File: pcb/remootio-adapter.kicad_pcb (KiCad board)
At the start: 2 copper layers, 110 x 60 mm, 63 parts, among them J1 AUX, J2 BATT, J3 ICSP, J4 Console, J5 SwitchIn, J6 SPM Connector, U1 remootio-3, U2 LM2940S-5.0, U3 AQV252GAX, U4 ATmega328PB-ANR, U5 ST232CDR, U6 AQV252GAX, U7 AQV252GAX, U8 AQV252GAX, Y1 CSTCE16M0V53-R0

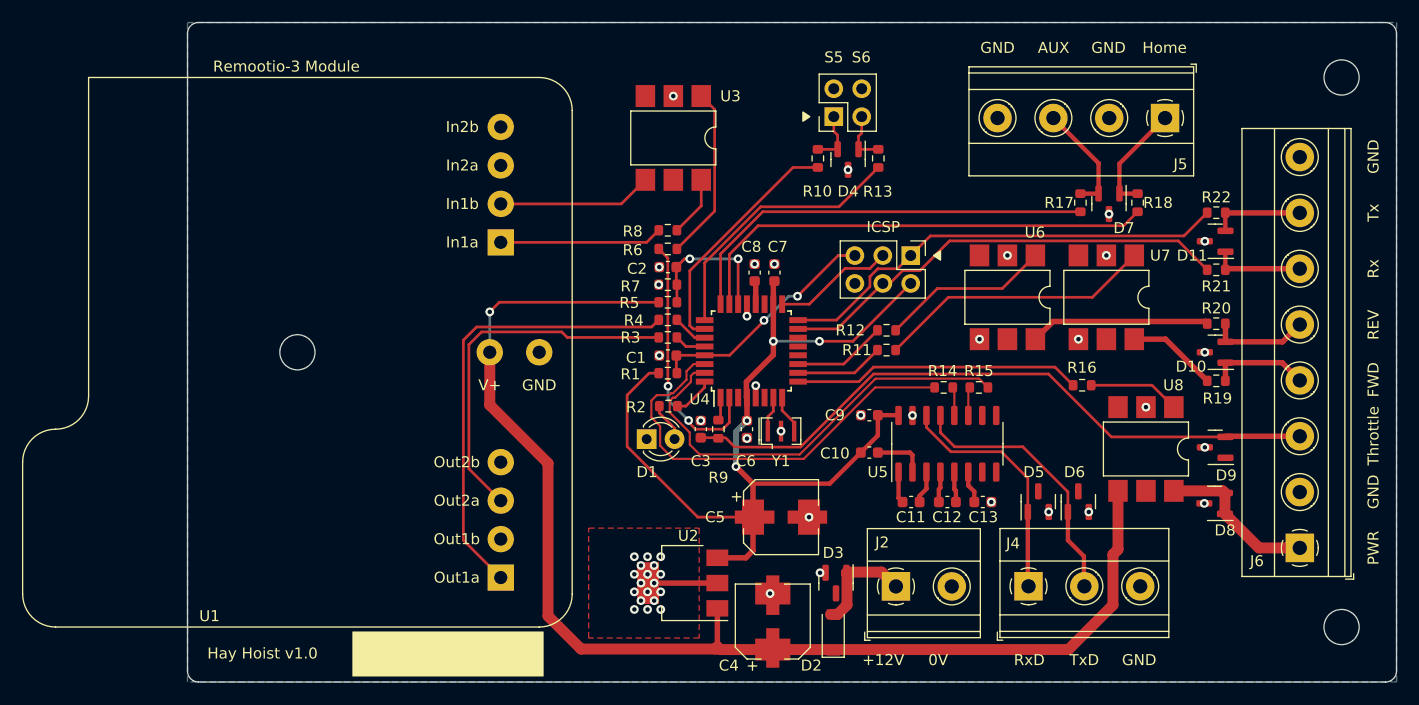
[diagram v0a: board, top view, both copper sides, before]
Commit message: Revise PCB layout for production board v1.1
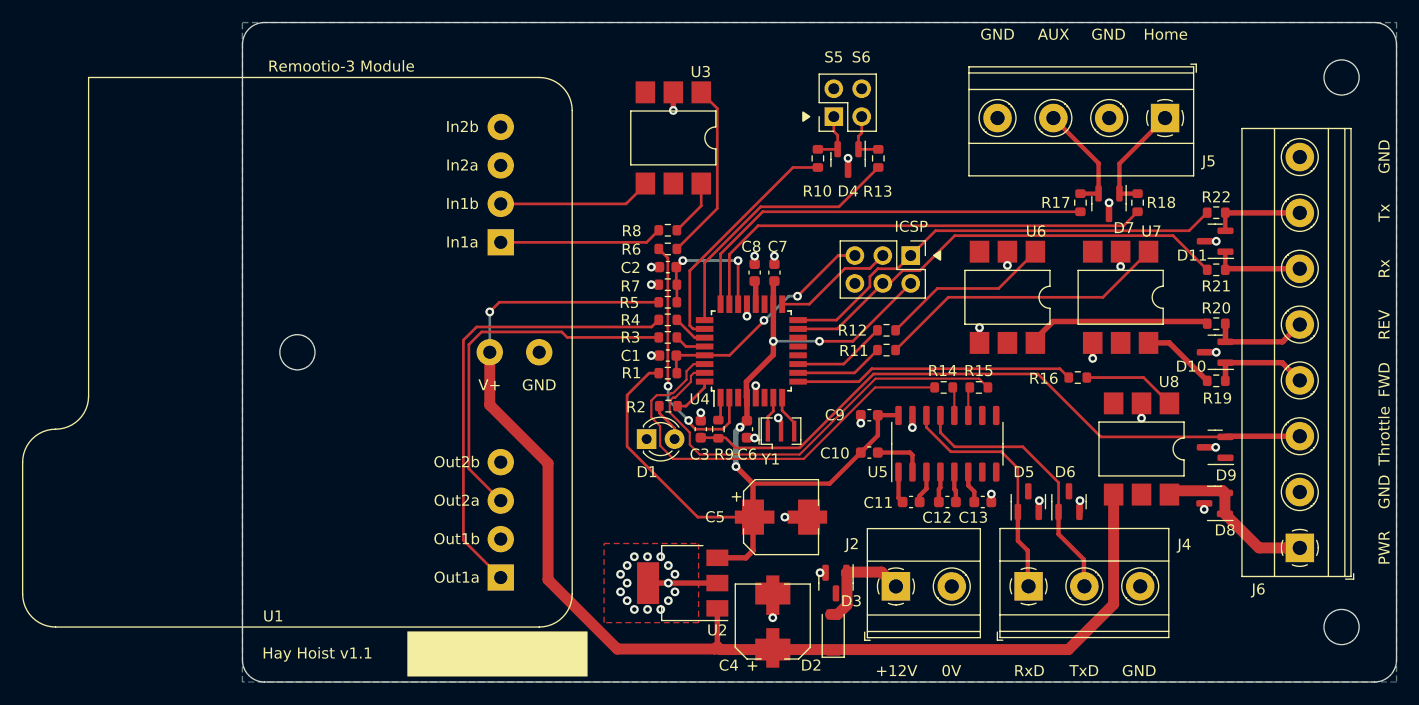
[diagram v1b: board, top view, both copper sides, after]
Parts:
- C1: value 1µ -> 100nF
- R1: value 1k -> 4.7k
- U3, U6, U7, U8: footprint Package_DIP:SMDIP-6_W7.62mm -> remootio-adapter:SMDIP-6_W7.62mm
- moved U7 1.30 mm to (156.9, 92.0)
- moved D5 0.91 mm to (148.5, 110.6)
- moved D6 0.85 mm to (152.2, 110.6)
- moved R16 0.81 mm to (153.0, 99.3)
- moved U8 0.40 mm to (158.8, 105.8)
- turned R1 to 0 degrees
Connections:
- R1 pad 1: RESET -> +5V
- R1 pad 2: +5V -> RESET
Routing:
- net GND: track 7.83 -> 36.6 mm, vias 48 -> 46
- net +12V: track 114.2 -> 111.8 mm
- net Net-(R19-Pad1): track 8.20 -> 6.76 mm
- net Net-(R11-Pad2): track 25.3 -> 26.7 mm
- net R3: track 26.3 -> 25.4 mm
- net Net-(R6-Pad2): track 15.8 -> 16.4 mm
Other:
- board size 110 x 60 mm -> 105 x 60 mm
- board text added: "Hay Hoist v1.1"
- board text removed: "Hay Hoist v1.0"

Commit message: Add mounting hole diagram
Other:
- board text added: "Antenna Clearance"
- board text added: "Connector Clearance"
- board text added: "M3"
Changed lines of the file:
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@@
   )
   (paper "A4")
+  (title_block
+    (title "Hay Hoist")
+    (date "2024-07-31")
+    (rev "1.1")
+    (company "Hyspec/6-v")
+  )
   (layers
     (0 "F.Cu" signal)
@@
   (gr_line (start 79 127) (end 180 127) (layer "Edge.Cuts") (width 0.1))
   (gr_line (start 77 69) (end 77 125) (layer "Edge.Cuts") (width 0.1))
+  (gr_line (start 82 96) (end 82 98) (layer "User.2") (width 0.15))
+  (gr_line (start 57 93) (end 64 86) (layer "User.2") (width 0.15))
+  (gr_line (start 164 133) (end 168 129) (layer "User.2") (width 0.15))
+  (gr_poly
+    (pts
+      (xy 189 134)
+      (xy 133 134)
+      (xy 133 128)
+      (xy 183 128)
+      (xy 183 66)
+      (xy 142 66)
+      (xy 142 60)
+      (xy 189 60)
+    ) (layer "User.2") (width 0.15) (fill none))
+  (gr_rect (start 55 70) (end 76 124) (layer "User.2") (width 0.15) (fill none))
+  (gr_line (start 158 133) (end 162 129) (layer "User.2") (width 0.15))
+  (gr_line (start 138 133) (end 140 131) (layer "User.2") (width 0.15))
+  (gr_line (start 176 122) (end 178 122) (layer "User.2") (width 0.15))
+  (gr_line (start 81 97) (end 83 97) (layer "User.2") (width 0.15))
+  (gr_circle (center 82 97) (end 84 97) (layer "User.2") (width 0.15) (fill none))
+  (gr_line (start 68 93) (end 73 88) (layer "User.2") (width 0.15))
+  (gr_circle (center 177 122) (end 179 122) (layer "User.2") (width 0.15) (fill none))
+  (gr_circle (center 177 72) (end 179 72) (layer "User.2") (width 0.15) (fill none))
+  (gr_line (start 177 121) (end 177 123) (layer "User.2") (width 0.15))
+  (gr_line (start 134 133) (end 138 129) (layer "User.2") (width 0.15))
+  (gr_line (start 70 81) (end 74 77) (layer "User.2") (width 0.15))
+  (gr_line (start 61 81) (end 70 72) (layer "User.2") (width 0.15))
+  (gr_rect (start 190 59) (end 54 135) (layer "User.2") (width 0.15) (fill none))
+  (gr_line (start 174 70) (end 173 69) (layer "User.2") (width 0.15))
+  (gr_line (start 84 99) (end 85 100) (layer "User.2") (width 0.15))
+  (gr_line (start 176 72) (end 178 72) (layer "User.2") (width 0.15))
+  (gr_line (start 175 124) (end 174 125) (layer "User.2") (width 0.15))
+  (gr_line (start 177 71) (end 177 73) (layer "User.2") (width 0.15))
+  (gr_line (start 57 77) (end 62 72) (layer "User.2") (width 0.15))
   (gr_text "S5" (at 130.8 70.1625) (layer "F.SilkS")
     (effects (font (size 1 1) (thickness 0.15)))
@@
     (effects (font (size 1 1) (thickness 0.15)))
   )
+  (gr_text "M3" (at 86 101) (layer "User.2")
+    (effects (font (size 1 1) (thickness 0.15)))
+  )
+  (gr_text "M3" (at 171 69) (layer "User.2")
+    (effects (font (size 1 1) (thickness 0.15)))
+  )
+  (gr_text "Connector Clearance" (at 149 131) (layer "User.2")
+    (effects (font (size 1 1) (thickness 0.15)))
+  )
+  (gr_text "M3" (at 172 126) (layer "User.2")
+    (effects (font (size 1 1) (thickness 0.15)))
+  )
+  (gr_text "Antenna Clearance" (at 66 83) (layer "User.2")
+    (effects (font (size 1 1) (thickness 0.15)))
+  )
+  (dimension (type aligned) (layer "User.2")
+    (pts (xy 177 135) (xy 190 135))
+    (height 3)
+    (gr_text "13.0 mm" (at 183.5 140) (layer "User.2")
+      (effects (font (size 1 1) (thickness 0.15)))
+    )
+    (format (units 3) (units_format 1) (precision 1))
+    (style (thickness 0.15) (arrow_length 1.27) (text_position_mode 2) (extension_height 0.58642) (extension_offset 0.5) keep_text_aligned)
+  )
+  (dimension (type aligned) (layer "User.2")
+    (pts (xy 54 59) (xy 54 135))
+    (height 5)
+    (gr_text "76.0 mm" (at 50 96 90) (layer "User.2")
+      (effects (font (size 1 1) (thickness 0.15)))
+    )
+    (format (units 3) (units_format 1) (precision 1))
+    (style (thickness 0.15) (arrow_length 1.27) (text_position_mode 2) (extension_height 0.58642) (extension_offset 0.5) keep_text_aligned)
+  )
+  (dimension (type aligned) (layer "User.2")
+    (pts (xy 190 122) (xy 190 97))
+    (height 6)
+    (gr_text "25.0 mm" (at 194 109.5 90) (layer "User.2")
+      (effects (font (size 1 1) (thickness 0.15)))
+    )
+    (format (units 3) (units_format 1) (precision 1))
+    (style (thickness 0.15) (arrow_length 1.27) (text_position_mode 2) (extension_height 0.58642) (extension_offset 0.5) keep_text_aligned)
+  )
+  (dimension (type aligned) (layer "User.2")
+    (pts (xy 177 135) (xy 82 135))
+    (height -5)
+    (gr_text "95.0 mm" (at 129.5 138.85) (layer "User.2")
+      (effects (font (size 1 1) (thickness 0.15)))
+    )
+    (format (units 3) (units_format 1) (precision 1))
+    (style (thickness 0.15) (arrow_length 1.27) (text_position_mode 0) (extension_height 0.58642) (extension_offset 0.5) keep_text_aligned)
+  )
+  (dimension (type aligned) (layer "User.2")
+    (pts (xy 190 135) (xy 190 122))
+    (height 4)
+    (gr_text "13.0 mm" (at 196 128.5 90) (layer "User.2")
+      (effects (font (size 1 1) (thickness 0.15)))
+    )
+    (format (units 3) (units_format 1) (precision 1))
+    (style (thickness 0.15) (arrow_length 1.27) (text_position_mode 2) (extension_height 0.58642) (extension_offset 0.5) keep_text_aligned)
+  )
+  (dimension (type aligned) (layer "User.2")
+    (pts (xy 54 59) (xy 190 59))
+    (height -4)
+    (gr_text "136.0 mm" (at 122 53.85) (layer "User.2")
+      (effects (font (size 1 1) (thickness 0.15)))
+    )
+    (format (units 3) (units_format 1) (precision 1))
+    (style (thickness 0.15) (arrow_length 1.27) (text_position_mode 0) (extension_height 0.58642) (extension_offset 0.5) keep_text_aligned)
+  )
+  (dimension (type aligned) (layer "User.2")
+    (pts (xy 82 135) (xy 54 135))
+    (height -3)
+    (gr_text "28.0 mm" (at 69 140) (layer "User.2")
+      (effects (font (size 1 1) (thickness 0.15)))
+    )
+    (format (units 3) (units_format 1) (precision 1))
+    (style (thickness 0.15) (arrow_length 1.27) (text_position_mode 2) (extension_height 0.58642) (extension_offset 0.5) keep_text_aligned)
+  )
+  (dimension (type aligned) (layer "User.2")
+    (pts (xy 190 59) (xy 190 67))
+    (height -2)
+    (gr_text "8.0 mm" (at 194 63 90) (layer "User.2")
+      (effects (font (size 1 1) (thickness 0.15)))
+    )
+    (format (units 3) (units_format 1) (precision 1))
+    (style (thickness 0.15) (arrow_length 1.27) (text_position_mode 2) (extension_height 0.58642) (extension_offset 0.5) keep_text_aligned)
+  )
   (segment (start 120.005112 124) (end 111.1 124) (width 1) (layer "F.Cu") (net 1))

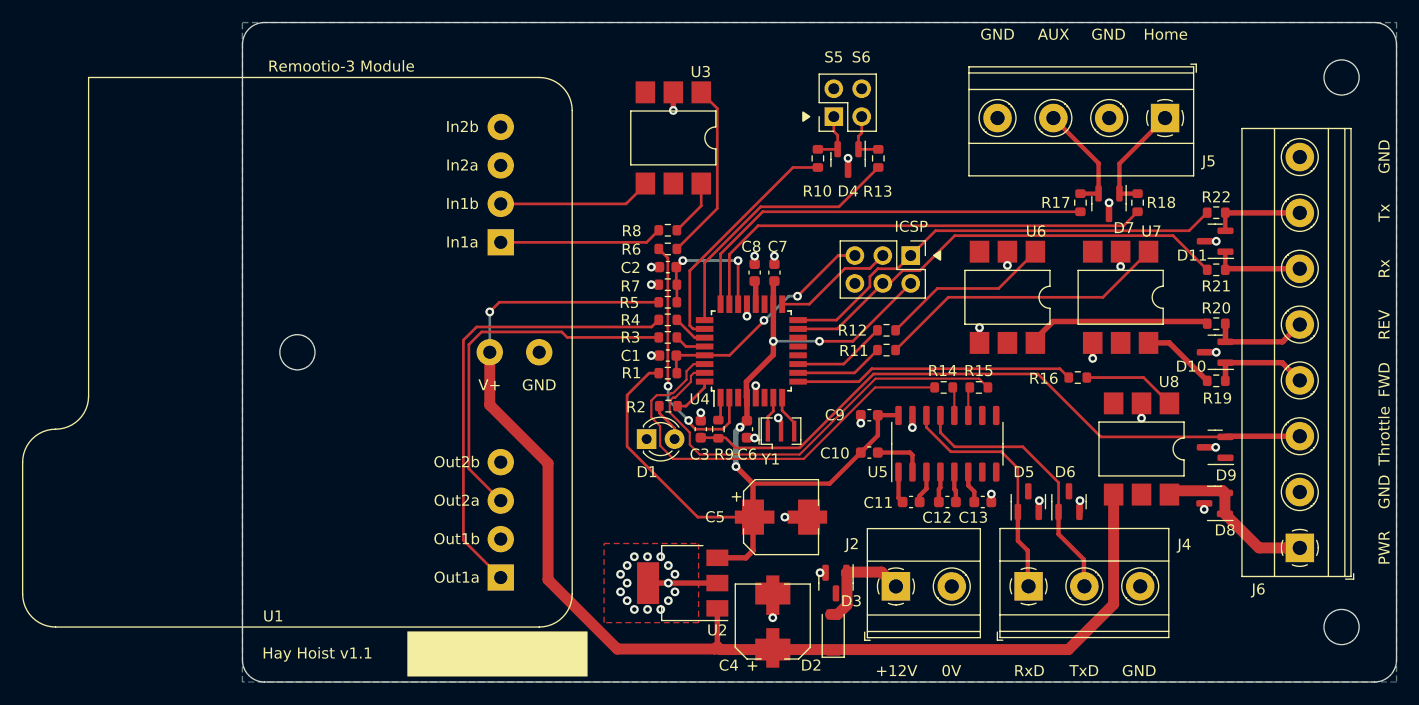
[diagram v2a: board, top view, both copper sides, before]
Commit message: Minor cosmetic footprint adjustment
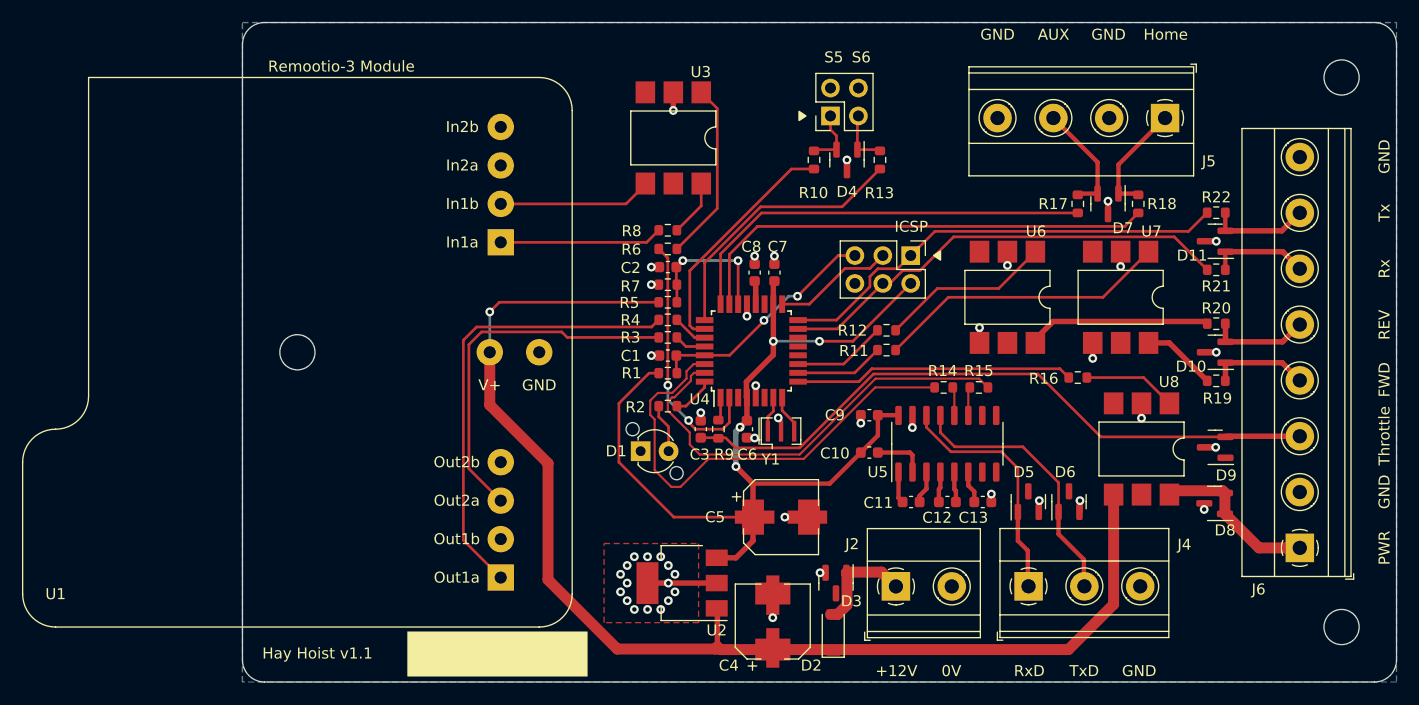
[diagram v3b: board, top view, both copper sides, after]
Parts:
- D1: footprint LED_THT:LED_D3.0mm_Clear -> remootio-adapter:bivar-led
- moved D1 1.32 mm to (114.5, 106.0)
- moved R10 0.38 mm to (129.0, 79.5)
- moved J1 0.31 mm to (130.5, 75.5)
- moved R17 0.26 mm to (153.0, 83.5)
- moved R13 0.20 mm to (135.0, 79.5)
- moved R18 0.13 mm to (158.5, 83.5)
- moved D4 0.11 mm to (132.0, 79.5)
- moved D7 0.09 mm to (155.8, 83.5)
- moved U2 0.06 mm to (117.0, 118.0)
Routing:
- net CRX: track 39.3 -> 43.1 mm
- net +5V: track 84.1 -> 85.5 mm
- net Net-(D1-Pad2): track 3.58 -> 4.47 mm
- net Net-(D11-Pad1): track 8.31 -> 9.04 mm
- net Net-(D11-Pad2): track 8.39 -> 9.08 mm

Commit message: Jostle footprints onto 0.5mm grid and change terminals to 5mm pitch
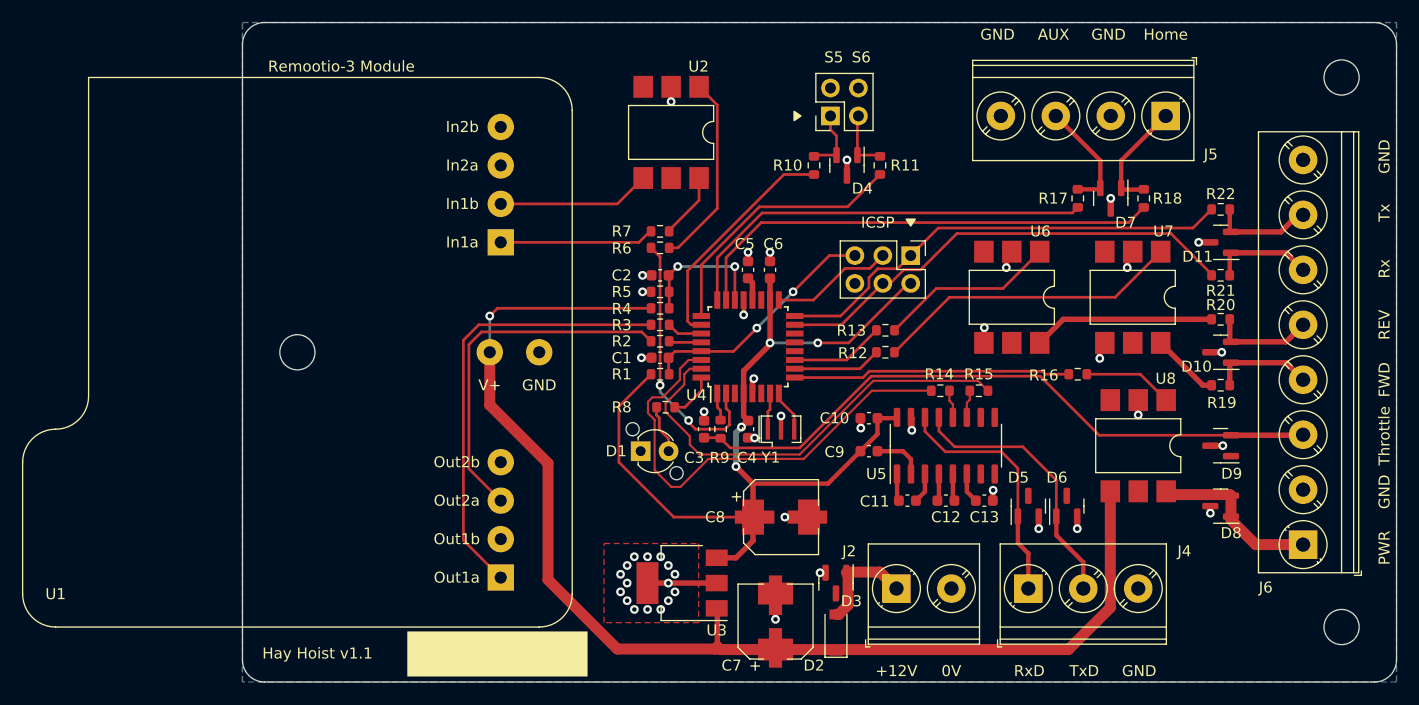
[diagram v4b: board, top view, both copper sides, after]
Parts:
- J2: footprint TerminalBlock_Phoenix:TerminalBlock_Phoenix_MKDS-1,5-2-5.08_1x02_P5.08mm_Horizontal -> TerminalBlock_Phoenix:TerminalBlock_Phoenix_PT-1,5-2-5.0-H_1x02_P5.00mm_Horizontal
- J4: footprint TerminalBlock_Phoenix:TerminalBlock_Phoenix_MKDS-1,5-3-5.08_1x03_P5.08mm_Horizontal -> TerminalBlock_Phoenix:TerminalBlock_Phoenix_PT-1,5-3-5.0-H_1x03_P5.00mm_Horizontal
- J5: footprint TerminalBlock_Phoenix:TerminalBlock_Phoenix_MKDS-1,5-4-5.08_1x04_P5.08mm_Horizontal -> TerminalBlock_Phoenix:TerminalBlock_Phoenix_PT-1,5-4-5.0-H_1x04_P5.00mm_Horizontal
- J6: footprint TerminalBlock_Phoenix:TerminalBlock_Phoenix_MKDS-1,5-8-5.08_1x08_P5.08mm_Horizontal -> TerminalBlock_Phoenix:TerminalBlock_Phoenix_PT-1,5-8-5.0-H_1x08_P5.00mm_Horizontal
- moved U7 1.10 mm to (158.0, 92.0)
- moved C2 1.03 mm to (115.0, 90.0)
- moved R5 0.96 mm to (115.0, 91.5)
- moved R4 0.89 mm to (115.0, 93.0)
- moved R3 0.83 mm to (115.0, 94.5)
- moved R2 0.78 mm to (115.0, 96.0)
- moved C1 0.73 mm to (115.0, 97.5)
- moved R1 0.71 mm to (115.0, 99.0)
- moved R6 0.71 mm to (115.0, 87.5)
- moved R7 0.71 mm to (115.0, 86.0)
- moved R18 0.71 mm to (159.0, 83.0)
- moved C5 0.65 mm to (123.0, 89.5)
- moved R21 0.64 mm to (166.0, 90.0)
- moved D8 0.60 mm to (166.0, 111.0)
- moved R19 0.57 mm to (166.0, 100.0)
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- renumbered C9 to C10, C6 to C4, C8 to C5, C7 to C6, C4 to C7, C5 to C8, C10 to C9, R13 to R11, R11 to R12, R12 to R13, R3 to R2, R4 to R3, R5 to R4, R7 to R5, R8 to R7, R2 to R8, U3 to U2, U2 to U3
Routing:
- net GND: track 36.6 -> 38.4 mm
- net Net-(R12-Pad2): track 26.7 -> 28.0 mm
- net Net-(R6-Pad2): track 16.4 -> 17.6 mm
- net R4: track 23.4 -> 24.4 mm
- net +12V: track 111.7 -> 110.7 mm
- net MTX: track 41.3 -> 42.2 mm
- net Net-(R3-Pad1): track 41.5 -> 40.7 mm
- net +5V: track 85.5 -> 84.7 mm
- net Net-(R7-Pad1): track 5.17 -> 5.87 mm
- net R4A: track 14.8 -> 14.1 mm
- net V1: track 1.85 -> 2.55 mm
- net RESET: track 21.6 -> 22.2 mm
- net MRX: track 41.8 -> 42.5 mm
- net Net-(C11-Pad1): track 2.88 -> 2.25 mm
- net A1: track 13.0 -> 12.4 mm
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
